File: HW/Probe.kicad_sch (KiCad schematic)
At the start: 33 parts, among them U1 NUCLEO-L432KC

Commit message: Update PCB
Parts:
- removed 100R2: R, Resistor_SMD:R_0603_1608Metric, symbol Device:R
- removed U1: NUCLEO-L432KC, MODULE_NUCLEO-L432KC, symbol NUCLEO-L432KC:NUCLEO-L432KC
- removed USB1: USB_C_Receptacle_USB2.0, KiCad:2171820001, symbol Connector:USB_C_Receptacle_USB2.0
- added Nucleo-L432KC1: ~, Library:MODULE_NUCLEO-L432KC, symbol Custom_Symbols:Nucleo-L432KC
- added R1: 100, Resistor_SMD:R_0603_1608Metric, symbol Device:R
- added R2, R3: 5.1K, Resistor_SMD:R_0603_1608Metric, symbol Device:R
- added USB1: USB4110-GF-A_REVB, GCT_USB4110-GF-A_REVB, symbol USB4110-GF-A_REVB:USB4110-GF-A_REVB
- CAM1: renamed from Camera1; footprint Connector_PinHeader_1.27mm:PinHeader_1x08_P1.27mm_Vertical -> Connector_PinSocket_2.54mm:PinSocket_1x08_P2.54mm_Vertical
- DIST1: renamed from Distance1; footprint Connector_PinHeader_1.27mm:PinHeader_1x05_P1.27mm_Vertical -> Connector_PinSocket_2.54mm:PinSocket_1x05_P2.54mm_Vertical
- H1, H10, H11, H12, H13, H14, H17, H18, H19, H2, H20, H3, H4, H5, H6, H7, H8, H9: footprint MountingHole:MountingHole_3.2mm_M3_Pad -> MountingHole:MountingHole_3.2mm_M3_Pad_Via
- renumbered LEDDriverOut1 to LED_OUT1, LEDDriverPower1 to LED_PWR1, LEDDriverSignal1 to LED_SIG1, Laser+1 to LSR+1, Laser-1 to LSR-1, LaserDriverOut1 to LSR_OUT1, LaserDriverPower1 to LSR_PWR1, LaserDriverSignal1 to LSR_SIG1
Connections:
- net +5V: now also Nucleo-L432KC1.5V, USB1.A4/B9 (VBUS), USB1.B4/A9 (VBUS)
- net CS: now also Nucleo-L432KC1.D3 (PB_0)
- net D+: now also Nucleo-L432KC1.D2 (PA_12), USB1.A6 (DP1), USB1.B6 (DP2)
- net D-: now also Nucleo-L432KC1.D10 (PA_11), USB1.A7 (DN1), USB1.B7 (DN2)
- net GND: now also Nucleo-L432KC1.GND, R2.1, R3.2, USB1.A1/B12 (GND), USB1.B1/A12 (GND), USB1.S1 (GND), USB1.S2 (GND), USB1.S3 (GND), USB1.S4 (GND)
- net MISO: now also Nucleo-L432KC1.A5 (PA6)
- net MOSI: now also Nucleo-L432KC1.A6 (PA7)
- net SCK: now also Nucleo-L432KC1.A4 (PA_5)
- net SCL: now also Nucleo-L432KC1.D1 (PA_9)
- net SDA: now also Nucleo-L432KC1.D0 (PA_10)
- net VSET_LASER: now also Nucleo-L432KC1.A7 (PA_2)
- net VSET_LED: now also Nucleo-L432KC1.D9 (PA_8)
- net 3V3 renamed +3.3V
- net +3.3V: now also Nucleo-L432KC1.3V3 (3v3), R1.1
- net DIST_INT renamed INT
- net INT: now also Nucleo-L432KC1.D6 (PB_1)
- new net: Nucleo-L432KC1.RST4 (NRST), R1.2
- new net: R2.2, USB1.A5 (CC1)
- new net: R3.1, USB1.B5 (CC2)
- no-connect marks 0 -> 16
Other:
- note added: "LED Driver"
- note added: "Laser Driver"
- note added: "Mounting Holes"
- note removed: "Nucleo Based Profilometer Breakout Board"
- moved on the sheet: CAM1, DIST1, H1, H10, H11, H12, H13, H14, H17, H18, H19, H2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

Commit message: Add title to sheets
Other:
- title: (none) -> Nucleo Based Profilometer Probe
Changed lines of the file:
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@@
 (kicad_sch (version 20230121) (generator eeschema)
   (paper "A4")
+  (title_block
+    (title "Nucleo Based Profilometer Probe")
+    (date "2023-04-19")
+    (rev "1.0")
+  )
   (junction (at 156.21 45.72) (diameter 0) (color 0 0 0 0)
   )

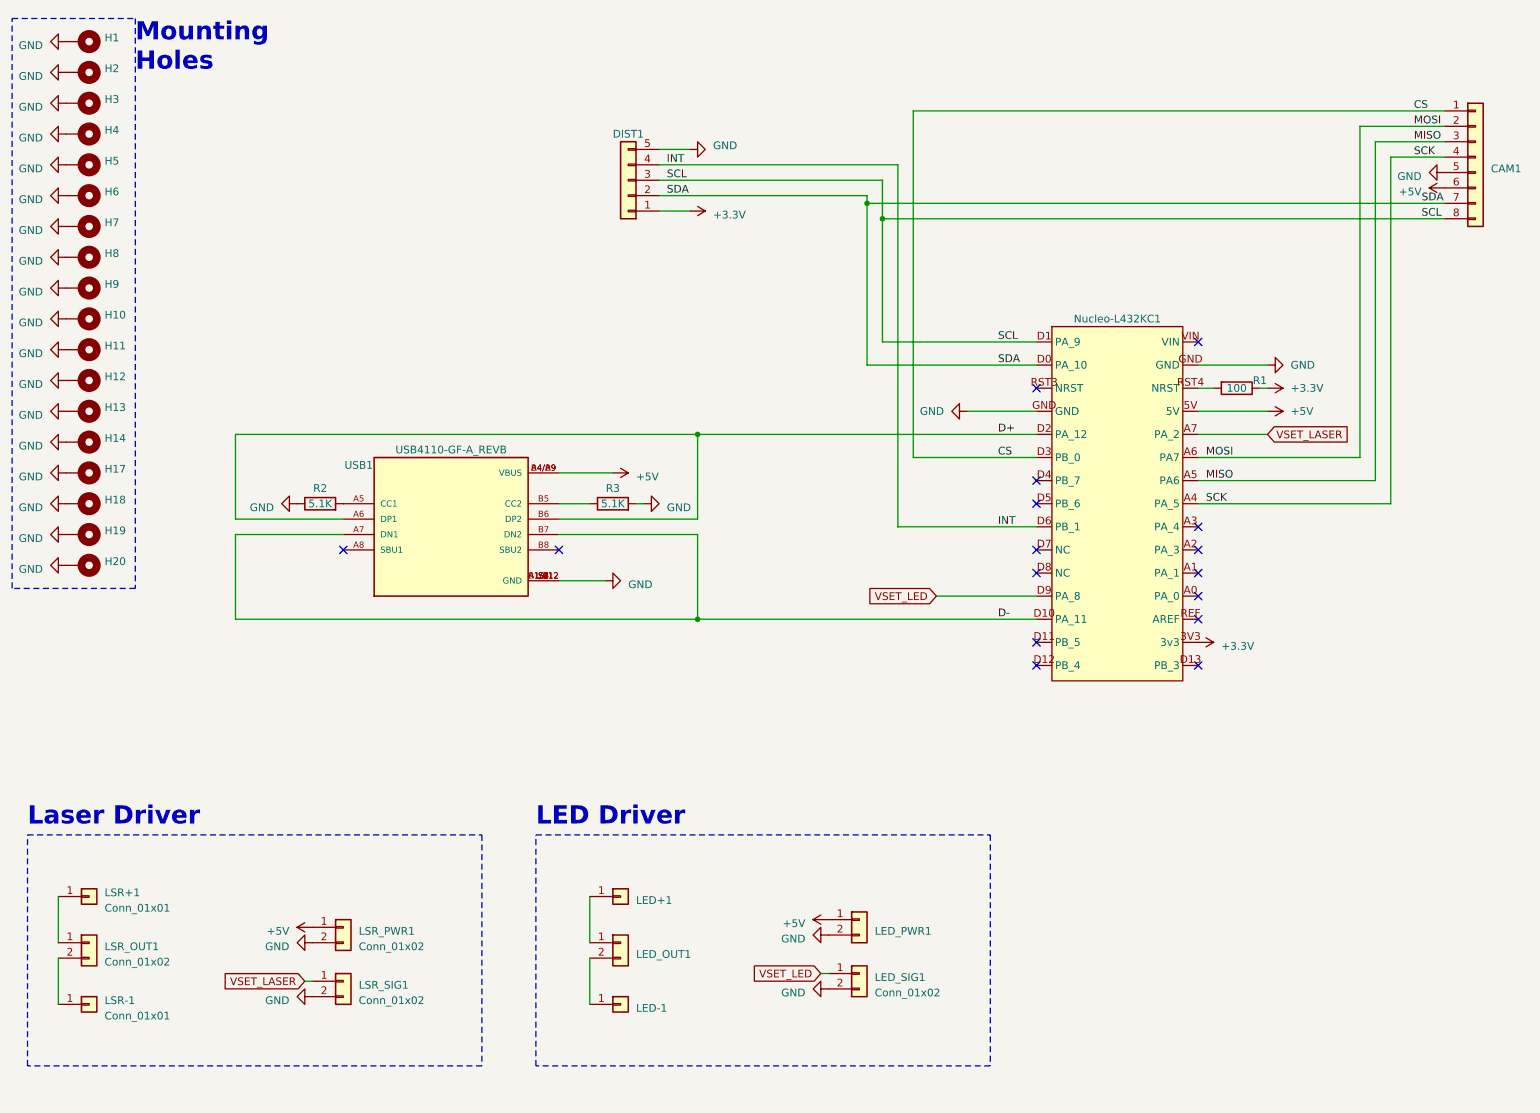
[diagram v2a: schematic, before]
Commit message: Change USB footprint, label PCB
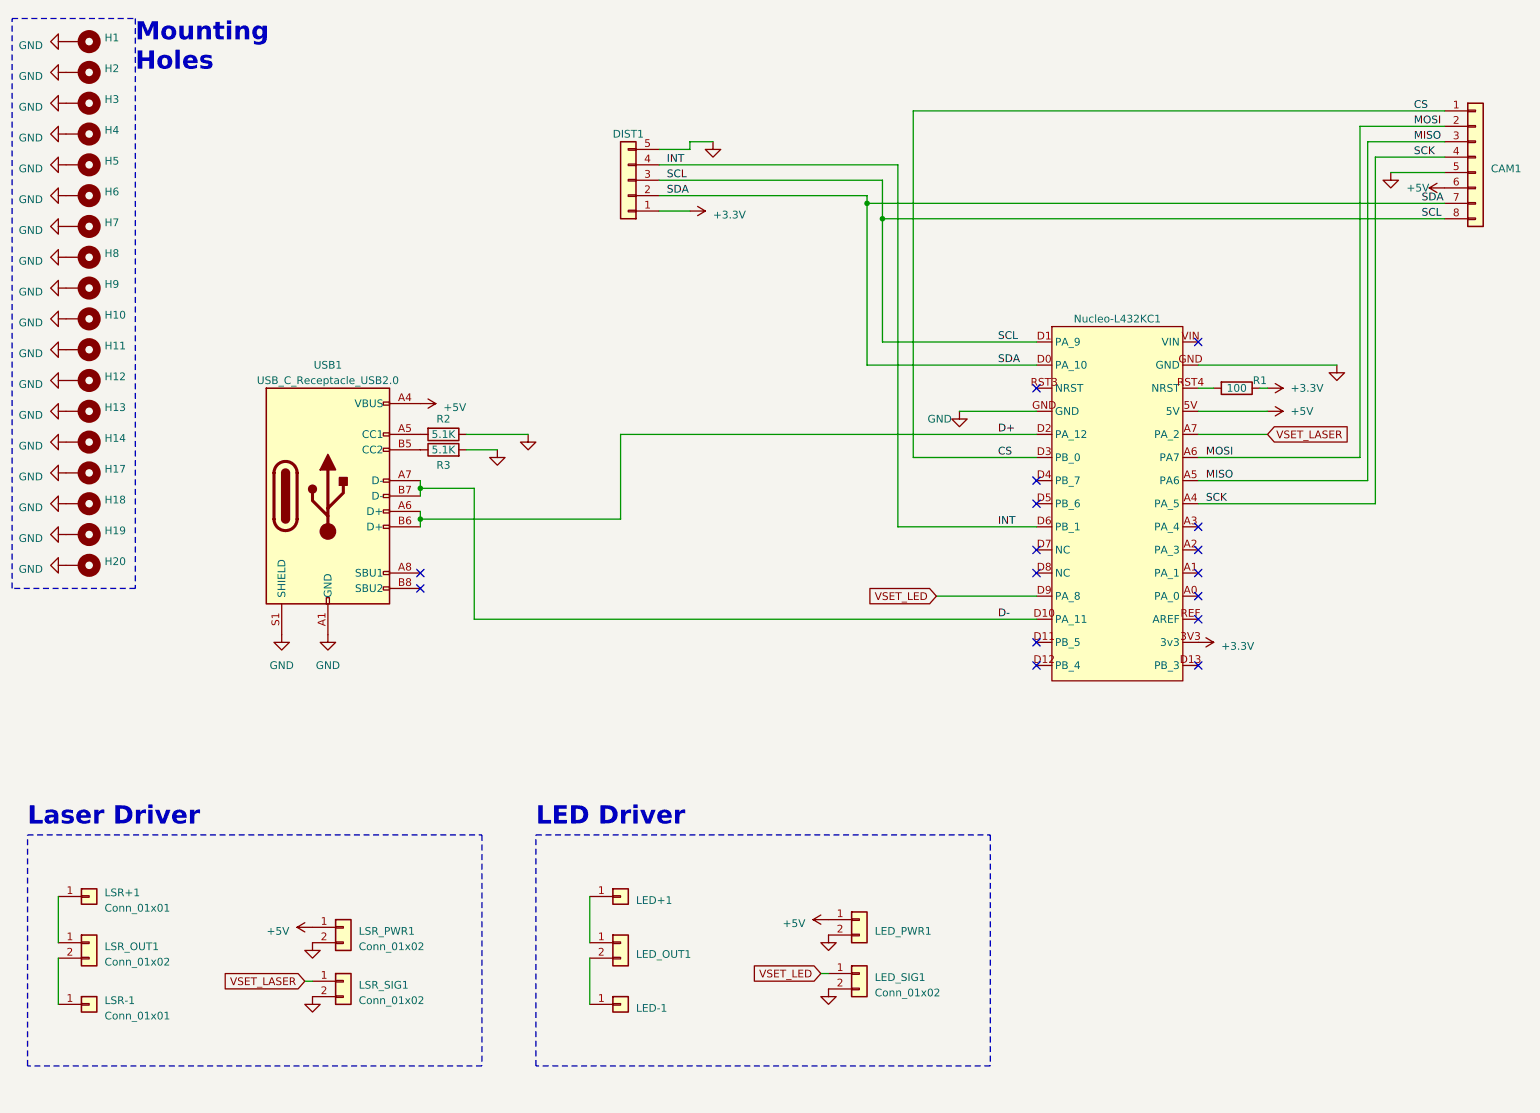
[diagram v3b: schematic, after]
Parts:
- removed USB1: USB4110-GF-A_REVB, GCT_USB4110-GF-A_REVB, symbol USB4110-GF-A_REVB:USB4110-GF-A_REVB
- added USB1: USB_C_Receptacle_USB2.0, Connector_USB:USB_C_Receptacle_HRO_TYPE-C-31-M-12, symbol Connector:USB_C_Receptacle_USB2.0
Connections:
- net +5V: now also USB1.A4 (VBUS), USB1.A9 (VBUS), USB1.B4 (VBUS), USB1.B9 (VBUS)
- net D+: now also USB1.A6 (D+), USB1.B6 (D+)
- net D-: now also USB1.A7 (D-), USB1.B7 (D-)
- net GND: now also USB1.A1 (GND), USB1.A12 (GND), USB1.B1 (GND), USB1.B12 (GND), USB1.S1 (SHIELD)
- net at R2.2: now also USB1.A5 (CC1)
- net at R3.1: now also USB1.B5 (CC2)
